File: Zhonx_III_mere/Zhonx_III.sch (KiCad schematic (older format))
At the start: 140 parts, among them K1 L_Motor, K2 R_Motor, K3 USART, P1 JTAG, Q1 FDV301N, Q2 FDV301N, U1 MCP73213, U10 BSL214N, U11 BSL214N, U12 24LC64T, U13 INA138, U14 STM32F405RGT6, U16 Line_1, U17 Line_2, U18 Line_3, U19 Line_4, U2 A3918_L, U20 Line_5, U3 A3918_R, U4 LTC2955CTS8-2, U5 SIB911DK, U6 SI1551DL, U7 LM2940, U8 MCP1700, U9 MCP1700, X1 QUARTZ_8Z

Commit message: Create Zhonx mere V2
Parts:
- removed R36: 100K, symbol R
- removed R37: 0.1 SHNT, symbol R
- removed R40, R41, R42, R43: 4,7K, symbol R
- removed U13: INA138, symbol INA138
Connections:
- net I_BAT is gone; now on net Enable_IR_Line: U14.16 (PA2/TIM5_CH3)
- net +8V: now also U5.6 (D1)
- net L_ENC_A: now also K1.6 (A)
- net L_ENC_B: now also K1.5 (B)
- net R_ENC_A: now also K2.5 (B)
- net R_ENC_B: now also K2.6 (A)
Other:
- note removed: "Amperemeter"
- moved on the sheet: ADXR1, C1, C10, C100, C101, C103, C104, C11, C12, C13, C14, C15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

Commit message: bluetooth passage en 4 couches
Signed-off-by: Jean-Paul <pacabot.jbe@gmail.com>
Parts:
- added R36: 100K, symbol R
- added R37: 0.1 SHNT, symbol R
- added U13: INA138, symbol INA138
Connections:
- net +3.3V: now also U13.5 (V+)
- net +8V: now also R37.1, U13.4 (Vin-); no longer U5.6 (D1)
- net Enable_IR_Line: no longer U14.16 (PA2/TIM5_CH3)
- net GND: now also R36.2, U13.2 (GND)
- new net: R37.2, U13.3 (Vin+), U5.6 (D1)
- new net I_BAT: R36.1, U13.1 (OUT), U14.16 (PA2/TIM5_CH3)
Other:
- note added: "Amperemeter"
- moved on the sheet: ADXR1, C1, C10, C100, C101, C103, C104, C11, C12, C13, C14, C15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

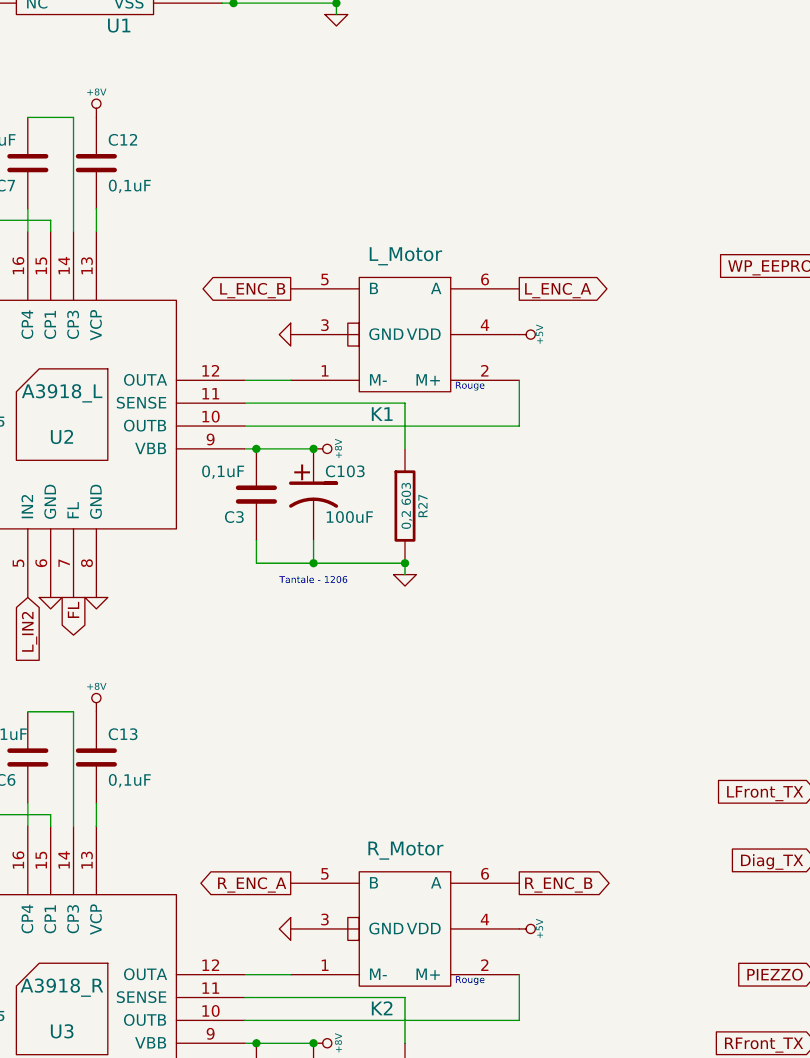
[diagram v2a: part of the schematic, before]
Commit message: mise a jour schéma carte mère (mesure courant, 4 résistances encodeurs)
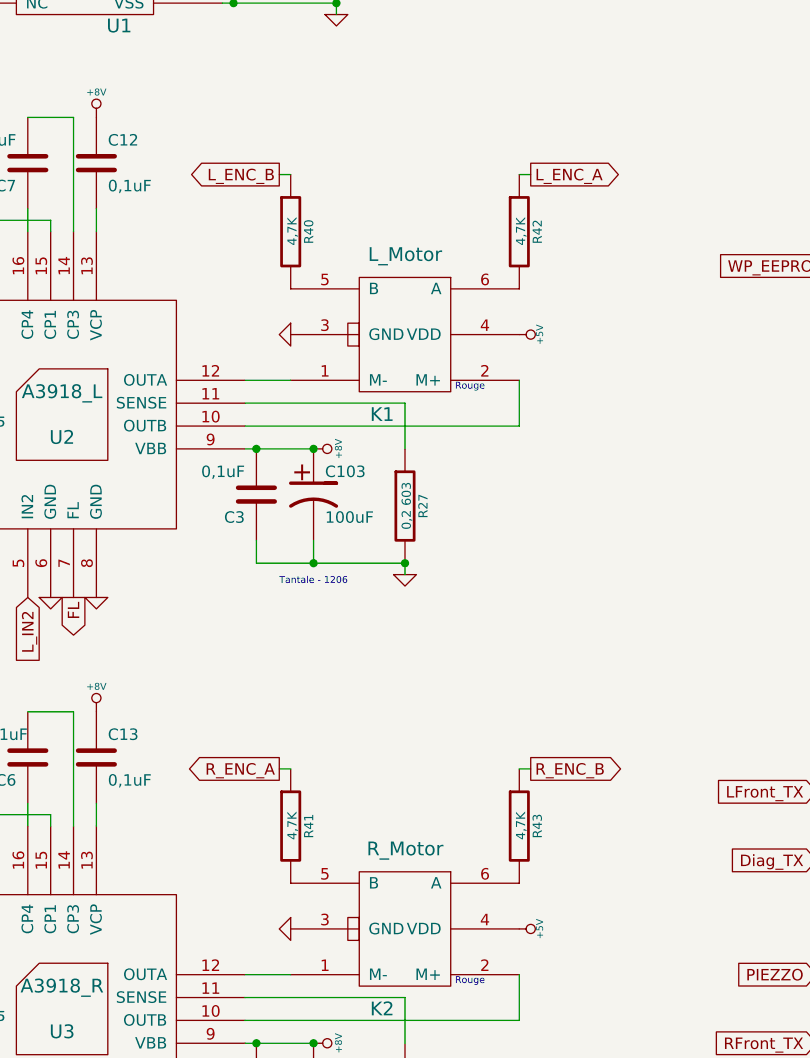
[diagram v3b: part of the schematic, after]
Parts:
- added R40, R41, R42, R43: 4,7K, symbol R
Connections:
- net L_ENC_A: now also R42.1; no longer K1.6 (A)
- net L_ENC_B: now also R40.1; no longer K1.5 (B)
- net R_ENC_A: now also R41.1; no longer K2.5 (B)
- net R_ENC_B: now also R43.1; no longer K2.6 (A)
- new net: K2.5 (B), R41.2
- new net: K2.6 (A), R43.2
- new net: K1.5 (B), R40.2
- new net: K1.6 (A), R42.2
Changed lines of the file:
@@
 Text GLabel 13850 2100 2    50   Input ~ 0
 R_ENC_B
-Text GLabel 4000 9350 2    50   Output ~ 0
+Text GLabel 4050 8850 2    50   Output ~ 0
 R_ENC_B
-Text GLabel 3000 9350 0    50   Output ~ 0
+Text GLabel 2950 8850 0    50   Output ~ 0
 R_ENC_A
-Text GLabel 3000 6750 0    50   Output ~ 0
+Text GLabel 2950 6250 0    50   Output ~ 0
 L_ENC_B
-Text GLabel 4000 6750 2    50   Output ~ 0
+Text GLabel 4050 6250 2    50   Output ~ 0
 L_ENC_A
 Text GLabel 800  8600 3    50   Input ~ 0
@@
 Text GLabel 10250 3800 0    50   Input ~ 0
 I_BAT
+$Comp
+L R R41
+U 1 1 54F22A8D
+P 3000 9100
+F 0 "R41" V 3080 9100 40  0000 C CNN
+F 1 "4,7K" V 3007 9101 40  0000 C CNN
+F 2 "" V 2930 9100 30  0000 C CNN
+F 3 "" H 3000 9100 30  0000 C CNN
+	1    3000 9100
+	1    0    0    -1
+$EndComp
+$Comp
+L R R43
+U 1 1 54F22B36
+P 4000 9100
+F 0 "R43" V 4080 9100 40  0000 C CNN
+F 1 "4,7K" V 4007 9101 40  0000 C CNN
+F 2 "" V 3930 9100 30  0000 C CNN
+F 3 "" H 4000 9100 30  0000 C CNN
+	1    4000 9100
+	1    0    0    -1
+$EndComp
+$Comp
+L R R42
+U 1 1 54F23207
+P 4000 6500
+F 0 "R42" V 4080 6500 40  0000 C CNN
+F 1 "4,7K" V 4007 6501 40  0000 C CNN
+F 2 "" V 3930 6500 30  0000 C CNN
+F 3 "" H 4000 6500 30  0000 C CNN
+	1    4000 6500
+	1    0    0    -1
+$EndComp
+$Comp
+L R R40
+U 1 1 54F2322A
+P 3000 6500
+F 0 "R40" V 3080 6500 40  0000 C CNN
+F 1 "4,7K" V 3007 6501 40  0000 C CNN
+F 2 "" V 2930 6500 30  0000 C CNN
+F 3 "" H 3000 6500 30  0000 C CNN
+	1    3000 6500
+	1    0    0    -1
+$EndComp
+Wire Wire Line
+	4000 6250 4050 6250
+Wire Wire Line
+	3000 6250 2950 6250
+Wire Wire Line
+	3000 8850 2950 8850
+Wire Wire Line
+	4000 8850 4050 8850
 $EndSCHEMATC
